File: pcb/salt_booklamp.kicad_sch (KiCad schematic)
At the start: 28 parts, among them J1 USB-C31-S-RA-CS1E-BK-T/R, P1 PIC-TC2050-IDC, U1 PIC16F15213-I/SN, U2 BQ21040DBVR, U3 TPS61158DRVR

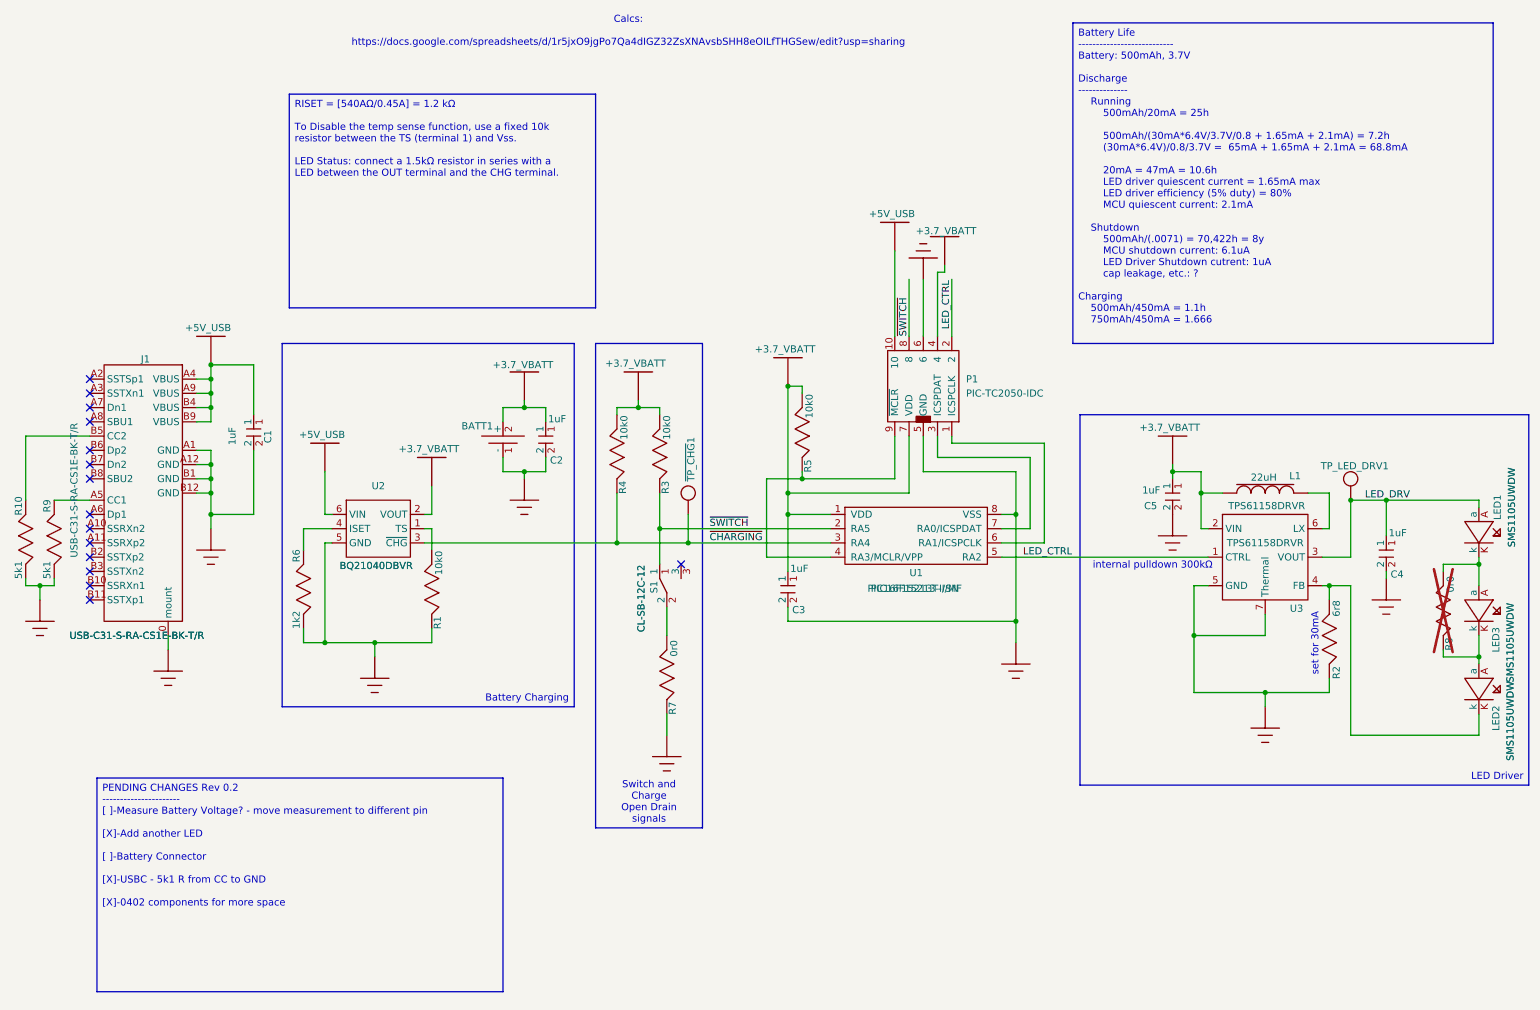
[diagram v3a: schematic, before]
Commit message: Moved battery voltage measurement to a different programming pin
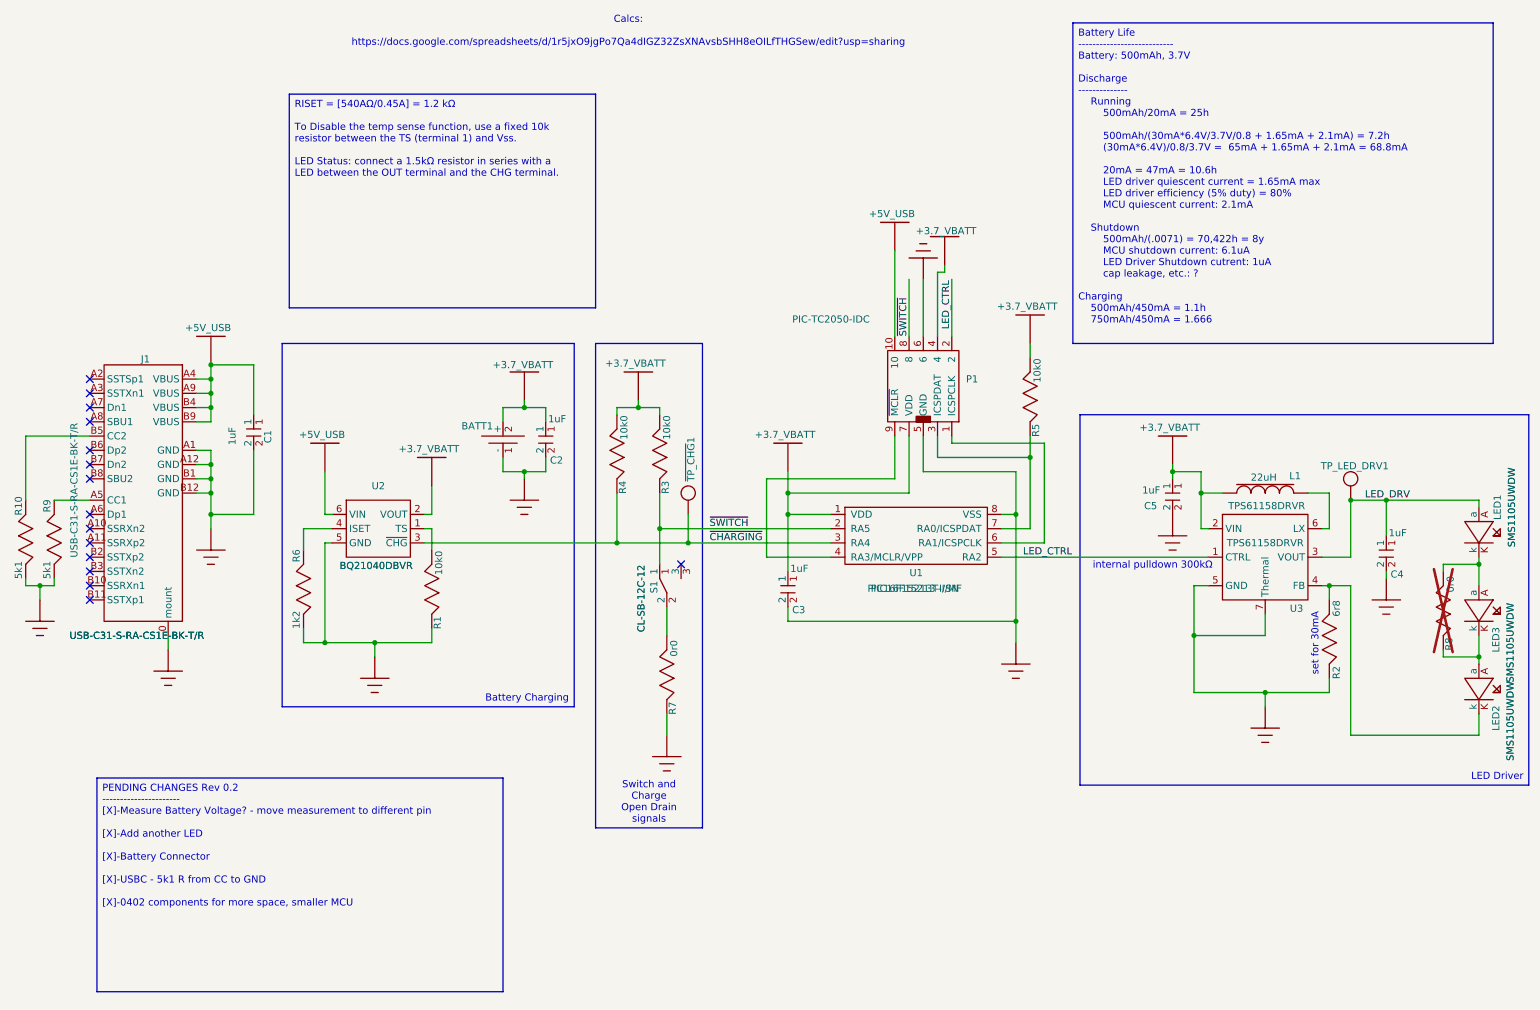
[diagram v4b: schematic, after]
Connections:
- net at P1.9 (~{MCLR}), U1.4 (RA3/MCLR/VPP): no longer R5.1
- net at P1.3 (ICSPDAT), U1.7 (RA0/ICSPDAT): now also R5.1
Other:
- moved on the sheet: R5
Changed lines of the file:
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@@
 		)
 	)
-	(text_box "PENDING CHANGES Rev 0.2\n----------------------\n[ ]-Measure Battery Voltage? - move measurement to different pin\n\n[X]-Add another LED\n\n[ ]-Battery Connector\n\n[X]-USBC - 5k1 R from CC to GND\n\n[X]-0402 components for more space\n\n"
+	(text_box "PENDING CHANGES Rev 0.2\n----------------------\n[X]-Measure Battery Voltage? - move measurement to different pin\n\n[X]-Add another LED\n\n[X]-Battery Connector\n\n[X]-USBC - 5k1 R from CC to GND\n\n[X]-0402 components for more space, smaller MCU\n\n"
 		(exclude_from_sim no)
 		(at 27.94 153.67 0)
@@
 	)
 	(junction
-		(at 151.13 83.82)
-		(diameter 0)
-		(color 0 0 0 0)
-	)
-	(junction
 		(at 191.77 125.73)
 		(diameter 0)
@@
 	)
 	(junction
-		(at 153.67 100.33)
-		(diameter 0)
-		(color 0 0 0 0)
-	)
-	(junction
 		(at 48.26 102.87)
 		(diameter 0)
@@
 		(color 0 0 0 0)
 	)
+	(junction
+		(at 194.31 96.52)
+		(diameter 0)
+		(color 0 0 0 0)
+	)
 	(no_connect
 		(at 26.67 90.17)
@@
 	(wire
 		(pts
-			(xy 151.13 83.82) (xy 151.13 102.87)
+			(xy 151.13 99.06) (xy 151.13 102.87)
 		)
 		(stroke
@@
 	(wire
 		(pts
-			(xy 153.67 85.09) (xy 153.67 83.82)
-		)
-		(stroke
-			(width 0)
-			(type default)
-		)
-	)
-	(wire
-		(pts
 			(xy 251.46 104.14) (xy 251.46 114.3)
 		)
@@
 	(wire
 		(pts
-			(xy 120.65 87.63) (xy 120.65 88.9)
+			(xy 194.31 92.71) (xy 194.31 96.52)
 		)
 		(stroke
@@
 	(wire
 		(pts
-			(xy 100.33 96.52) (xy 100.33 99.06)
+			(xy 120.65 87.63) (xy 120.65 88.9)
 		)
 		(stroke
@@
 	(wire
 		(pts
-			(xy 153.67 100.33) (xy 170.18 100.33)
+			(xy 100.33 96.52) (xy 100.33 99.06)
 		)
 		(stroke
@@
 	(wire
 		(pts
+			(xy 194.31 76.2) (xy 194.31 78.74)
+		)
+		(stroke
+			(width 0)
+			(type default)
+		)
+	)
+	(wire
+		(pts
 			(xy 77.47 129.54) (xy 77.47 132.08)
 		)
@@
 	(wire
 		(pts
-			(xy 224.79 102.87) (xy 224.79 109.22)
+			(xy 147.32 100.33) (xy 170.18 100.33)
 		)
 		(stroke
@@
 	(wire
 		(pts
-			(xy 48.26 80.01) (xy 55.88 80.01)
+			(xy 224.79 102.87) (xy 224.79 109.22)
 		)
 		(stroke
@@
 	(wire
 		(pts
-			(xy 247.65 119.38) (xy 246.38 119.38)
+			(xy 48.26 80.01) (xy 55.88 80.01)
 		)
 		(stroke
@@
 	(wire
 		(pts
-			(xy 153.67 83.82) (xy 151.13 83.82)
+			(xy 247.65 119.38) (xy 246.38 119.38)
 		)
 		(stroke
@@
 	(wire
 		(pts
-			(xy 153.67 99.06) (xy 153.67 100.33)
-		)
-		(stroke
-			(width 0)
-			(type default)
-		)
-	)
-	(wire
-		(pts
 			(xy 64.77 113.03) (xy 64.77 109.22)
 		)
@@
 	(wire
 		(pts
-			(xy 147.32 100.33) (xy 153.67 100.33)
-		)
-		(stroke
-			(width 0)
-			(type default)
-		)
-	)
-	(wire
-		(pts
 			(xy 124.46 86.36) (xy 124.46 87.63)
 		)
@@
 			"AAAAAAAAAAAAAAAAAAAAAAAAAAAAAAAAAAAAAAAAAAAAAAAAAAAAAAAAAAAAAAAAAAAAAAAAAAAA"
 			"AAAAAAAAAAAAAAAAAAAAAAAAAAAAAAAAAAAAAAAAAAAAAAAAAAAAAAAAAAAAAAAAAAAAAAAAAAAA"
+			"AAAAAAAAAAAAAAAAAAAAAAAAAAAAAAAAAAAAAAAAAAAAAAAAAAAAAAAAAAAAAAAAAAAAAAAAAAAA"
+			"AAAAAAAAAAAAAAAAAAAAAAAAAAAAAAAAAAAAAAAAAAAAAAAAAAAAAAAAAAAAAAAAAAAAAAAAAAAA"
+			"AAAAAAAAAAAAAAAAAAAAAAAAAAAAAAAAAAAAAAAAAAAAAAAAAAAAAAAAAAAAAAAAAAAAAAAAAAAA"
+			"AAAAAAAAAAAAAAAAAAAAAAAAAAAAAAAAAAAAAAAAAAAAAAAAAAAAAAAAAAAAAAAAAAAAAAAAAAAA"
+			"AAAAAAAAAAAAAAAAAAAAAAAAAAAAAAAAAAAAAAAAAAAAAAAAAAAAAAAAAAAAAAAAAAAAAAAAAAAA"
+			"AAAAAAAAAAAAAAAAAAAAAAAAAAAAAAAAAAAAAAAAAAAAAAAAAAAAAAAAAAAAAAAAAAAAAAAAAAAA"
+			"AAAAAAAAAAAAAAAAAAAAAAAAAAAAAAAAAAAAAAAAAAAAAAAAAAAAAAAAAAAAAAAAAAAAAAAAAAAA"
+			"AAAAAAAAAAAAAAAAAAAAAAAAAAAAAAAAAAAAAAAAAAAAAAAAAAAAAAAAAAAAAAAAAAAAAAAAAAAA"
+			"AAAAAAAAAAAAAAAAAAAAAAAAAAAAAAAAAAAAAAAAAAAAAAAAAAAAAAAAAAAAAAAAAAAAAAAAAAAA"
+			"AAAAAAAAAAAAAAAAAAAAAAAAAAAAAAAAAAAAAAAAAAAAAAAAAAAAAAAAAAAAAAAAAAAAAAAAAAAA"
+			"AAAAAAAAAAAAAAAAAAAAAAAAAAAAAAAAAAAAAAAAAAAAAAAAAAAAAAAAAAAAAAAAAAAAAAAAAAAA"
+			"AAAAAAAAAAAAAAAAAAAAAAAAAAAAAAAAAAAAAAAAAAAAAAAAAAAAAAAAAAAAAAAAAAAAAAAAAAAA"
+			"AAAAAAAAAAAAAAAAAAAAAAAAAAAAAAAAAAAAAAAAAAAAAAAAAAAAAAAAAAAAAAAAAAAAAAAAAAAA"
+			"AAAAAAAAAAAAAAAAAAAAAAAAAAAAAAAAAAAAAAAAAAAAAAAAAAAAAAAAAAAAAAAAAAAAAAAAAAAA"
+			"AAAAAAAAAAAAAAAAAAAAAAAAAAAAAAAAAAAAAAAAAAAAAAAAAAAAAAAAAAAAAAAAAAAAAAAAAAAA"
+			"AAAAAAAAAAAAAAAAAAAAAAAAAAAAAAAAAAAAAAAAAAAAAAAAAAAAAAAAAAAAAAAAAAAAAAAAAAAA"
+			"AAAAAAAAAAAAAAAAAAAAAAAAAAAAAAAAAAAAAAAAAAAAAAAAAAAAAAAAAAAAAAAAAAAAAAAAAAAA"
+			"AAAAAAAAAAAAAAAAAAAAAAAAAAAAAAAAAAAAAAAAAAAAAAAAAAAAAAAAAAAAAAAAAAAAAAAAAAAA"
 			"AAAAAAAAAA=="
 		)
@@
 		(lib_name "resistor_3")
 		(lib_id "salt_booklamp:resistor")
-		(at 153.67 91.44 90)
+		(at 194.31 85.09 90)
 		(unit 1)
 		(exclude_from_sim yes)
@@
 		(dnp no)
 		(property "Reference" "R5"
-			(at 154.686 98.044 0)
+			(at 195.326 91.694 0)
 			(effects
 				(font
@@
 		)
 		(property "Value" "10k0"
-			(at 154.94 87.376 0)
+			(at 195.58 81.026 0)
 			(effects
 				(font
@@
 		)
 		(property "Footprint" "Resistor_SMD:R_0402_1005Metric"
-			(at 158.75 91.44 0)
+			(at 199.39 85.09 0)
 			(effects
 				(font
@@
 		)
 		(property "Datasheet" ""
-			(at 153.67 91.44 0)
+			(at 194.31 85.09 0)
 			(effects
 				(font
@@
 		)
 		(property "Description" "RES 10K OHM 1% 1/10W 0603"
-			(at 153.67 91.44 0)
+			(at 194.31 85.09 0)
 			(effects
 				(font
@@
 		)
 		(property "Manufacturer Part Number" "RMCF0603FT10K0"
-			(at 153.67 91.44 0)
+			(at 194.31 85.09 0)
 			(effects
 				(font
@@
 		(on_board yes)
 		(dnp no)
-		(fields_autoplaced yes)
 		(property "Reference" "P1"
 			(at 182.88 82.5499 0)
@@
 		)
 		(property "Value" "PIC-TC2050-IDC"
-			(at 182.88 85.0899 0)
+			(at 151.892 71.882 0)
 			(effects
 				(font
@@
 	)
 	(symbol
+		(lib_id "salt_booklamp:Power")
+		(at 194.31 71.12 0)
+		(unit 1)
+		(exclude_from_sim yes)
+		(in_bom yes)
+		(on_board yes)
+		(dnp no)
+		(property "Reference" "#PWR021"
+			(at 192.786 72.39 0)
+			(effects
+				(font
+					(size 1.27 1.27)
+				)
+				(hide yes)
+			)
+		)
+		(property "Value" "+3.7_VBATT"
+			(at 193.802 69.596 0)
+			(effects
+				(font
+					(size 1.27 1.27)
+				)
+			)
+		)
+		(property "Footprint" ""
+			(at 194.31 71.12 0)
+			(effects
+				(font
+					(size 1.27 1.27)
+				)
+				(hide yes)
+			)
+		)
+		(property "Datasheet" ""
+			(at 194.31 71.12 0)
+			(effects
+				(font
+					(size 1.27 1.27)
+				)
+				(hide yes)
+			)
+		)
+		(property "Description" ""
+			(at 194.31 71.12 0)
+			(effects
+				(font
+					(size 1.27 1.27)
+				)
+				(hide yes)
+			)
+		)
+		(pin ""
+		)
+		(instances
+			(project "salt_booklamp"
+				(path "/991f2cc7-99ce-452c-919d-a53cd26a4b08"
+					(reference "#PWR021")
+					(unit 1)
+				)
+			)
+		)
+	)
+	(symbol
 		(lib_id "salt_booklamp:1-Pin_Header")
 		(at 133.35 102.87 0)
@@
 	(symbol
 		(lib_id "salt_booklamp:Power")
-		(at 151.13 78.74 0)
+		(at 151.13 93.98 0)
 		(unit 1)
 		(exclude_from_sim yes)
@@
 		(dnp no)
 		(property "Reference" "#PWR09"
-			(at 149.606 80.01 0)
+			(at 149.606 95.25 0)
 			(effects
 				(font
@@
 		)
 		(property "Value" "+3.7_VBATT"
-			(at 150.622 77.216 0)
+			(at 150.622 92.456 0)
 			(effects
 				(font
@@
 		)
 		(property "Footprint" ""
-			(at 151.13 78.74 0)
+			(at 151.13 93.98 0)
 			(effects
 				(font
@@
 		)
 		(property "Datasheet" ""
-			(at 151.13 78.74 0)
+			(at 151.13 93.98 0)
 			(effects
 				(font
@@
 		)
 		(property "Description" ""
-			(at 151.13 78.74 0)
+			(at 151.13 93.98 0)
 			(effects
 				(font

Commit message: Placement work
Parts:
- U1: value PIC16F15213-I/SN -> PIC16F15213T-I/MF
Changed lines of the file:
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@@
 			"AAAAAAAAAAAAAAAAAAAAAAAAAAAAAAAAAAAAAAAAAAAAAAAAAAAAAAAAAAAAAAAAAAAAAAAAAAAA"
 			"AAAAAAAAAAAAAAAAAAAAAAAAAAAAAAAAAAAAAAAAAAAAAAAAAAAAAAAAAAAAAAAAAAAAAAAAAAAA"
+			"AAAAAAAAAAAAAAAAAAAAAAAAAAAAAAAAAAAAAAAAAAAAAAAAAAAAAAAAAAAAAAAAAAAAAAAAAAAA"
+			"AAAAAAAAAAAAAAAAAAAAAAAAAAAAAAAAAAAAAAAAAAAAAAAAAAAAAAAAAAAAAAAAAAAAAAAAAAAA"
+			"AAAAAAAAAAAAAAAAAAAAAAAAAAAAAAAAAAAAAAAAAAAAAAAAAAAAAAAAAAAAAAAAAAAAAAAAAAAA"
+			"AAAAAAAAAAAAAAAAAAAAAAAAAAAAAAAAAAAAAAAAAAAAAAAAAAAAAAAAAAAAAAAAAAAAAAAAAAAA"
+			"AAAAAAAAAAAAAAAAAAAAAAAAAAAAAAAAAAAAAAAAAAAAAAAAAAAAAAAAAAAAAAAAAAAAAAAAAAAA"
+			"AAAAAAAAAAAAAAAAAAAAAAAAAAAAAAAAAAAAAAAAAAAAAAAAAAAAAAAAAAAAAAAAAAAAAAAAAAAA"
+			"AAAAAAAAAAAAAAAAAAAAAAAAAAAAAAAAAAAAAAAAAAAAAAAAAAAAAAAAAAAAAAAAAAAAAAAAAAAA"
+			"AAAAAAAAAAAAAAAAAAAAAAAAAAAAAAAAAAAAAAAAAAAAAAAAAAAAAAAAAAAAAAAAAAAAAAAAAAAA"
+			"AAAAAAAAAAAAAAAAAAAAAAAAAAAAAAAAAAAAAAAAAAAAAAAAAAAAAAAAAAAAAAAAAAAAAAAAAAAA"
+			"AAAAAAAAAAAAAAAAAAAAAAAAAAAAAAAAAAAAAAAAAAAAAAAAAAAAAAAAAAAAAAAAAAAAAAAAAAAA"
+			"AAAAAAAAAAAAAAAAAAAAAAAAAAAAAAAAAAAAAAAAAAAAAAAAAAAAAAAAAAAAAAAAAAAAAAAAAAAA"
+			"AAAAAAAAAAAAAAAAAAAAAAAAAAAAAAAAAAAAAAAAAAAAAAAAAAAAAAAAAAAAAAAAAAAAAAAAAAAA"
+			"AAAAAAAAAAAAAAAAAAAAAAAAAAAAAAAAAAAAAAAAAAAAAAAAAAAAAAAAAAAAAAAAAAAAAAAAAAAA"
+			"AAAAAAAAAAAAAAAAAAAAAAAAAAAAAAAAAAAAAAAAAAAAAAAAAAAAAAAAAAAAAAAAAAAAAAAAAAAA"
+			"AAAAAAAAAAAAAAAAAAAAAAAAAAAAAAAAAAAAAAAAAAAAAAAAAAAAAAAAAAAAAAAAAAAAAAAAAAAA"
+			"AAAAAAAAAAAAAAAAAAAAAAAAAAAAAAAAAAAAAAAAAAAAAAAAAAAAAAAAAAAAAAAAAAAAAAAAAAAA"
+			"AAAAAAAAAAAAAAAAAAAAAAAAAAAAAAAAAAAAAAAAAAAAAAAAAAAAAAAAAAAAAAAAAAAAAAAAAAAA"
+			"AAAAAAAAAAAAAAAAAAAAAAAAAAAAAAAAAAAAAAAAAAAAAAAAAAAAAAAAAAAAAAAAAAAAAAAAAAAA"
 			"AAAAAAAAAA=="
 		)
@@
 			)
 		)
-		(property "Value" "PIC16F15213-I/SN"
-			(at 173.736 119.888 0)
+		(property "Value" "PIC16F15213T-I/MF"
+			(at 173.482 122.428 0)
 			(effects
 				(font
@@
 			)
 		)
-		(property "Description" "PIC PIC® 16F, Functional Safety (FuSa) Microcontroller IC 8-Bit 32MHz 3.5KB (2K x 14) FLASH 8-SOIC"
+		(property "Description" "PIC PIC® 16F, Functional Safety (FuSa) Microcontroller IC 8-Bit 32MHz 3.5KB (2K x 14) FLASH 8-DFN (3x3)"
 			(at 173.99 110.49 0)
 			(effects

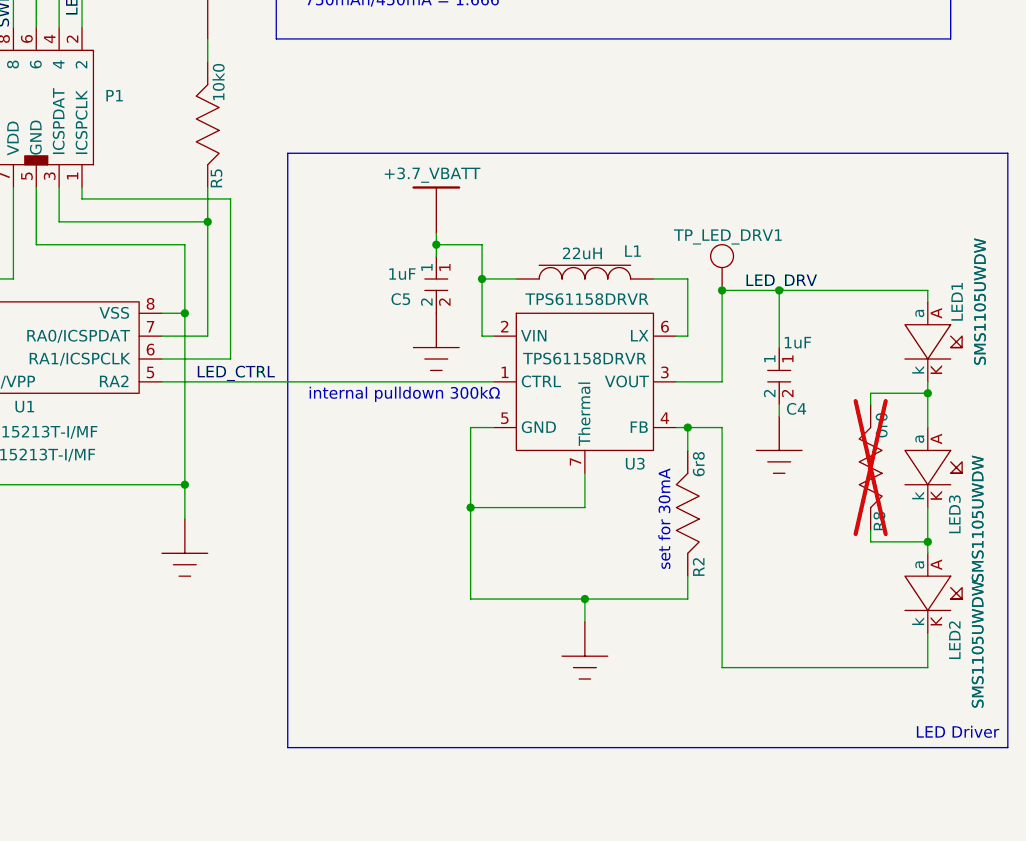
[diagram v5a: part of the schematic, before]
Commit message: adjust net classes and start routing
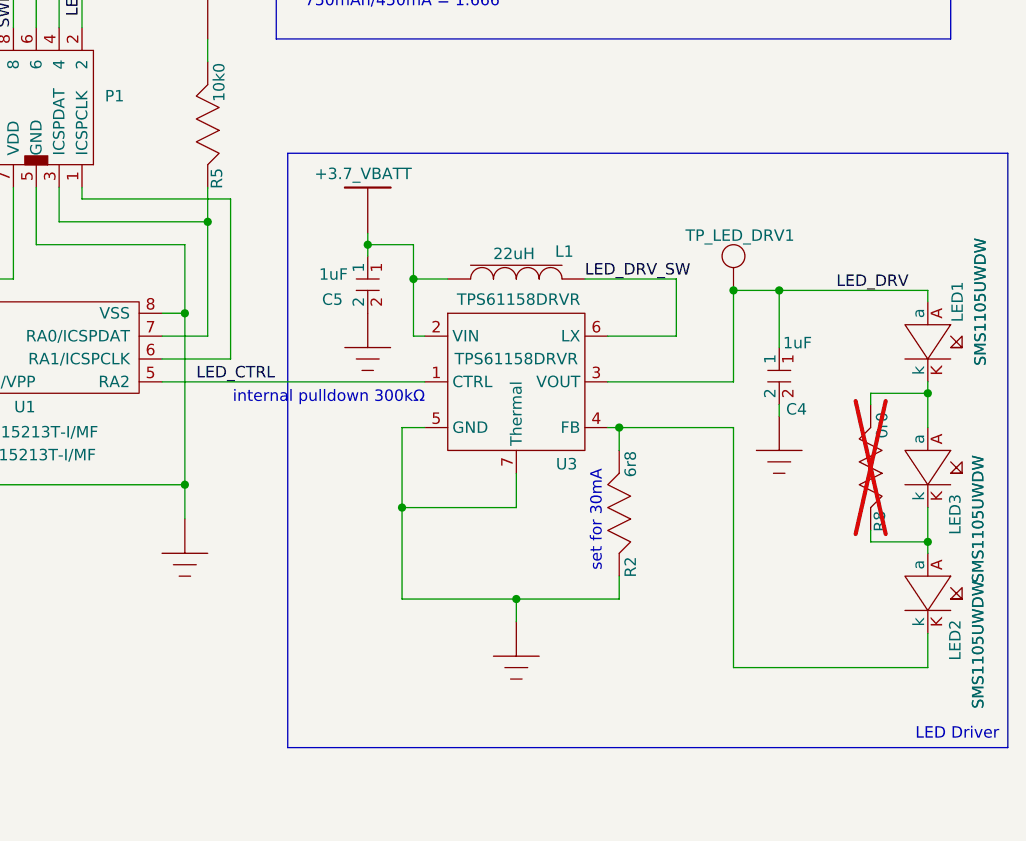
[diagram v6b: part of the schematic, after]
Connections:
- net LED_DRV_SW: now reaches L1.2, U3.6 (LX)
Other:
- moved on the sheet: C5, L1, R2, TP_LED_DRV1, U3
